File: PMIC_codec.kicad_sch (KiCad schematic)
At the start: 18 parts, among them U5 RK809-2

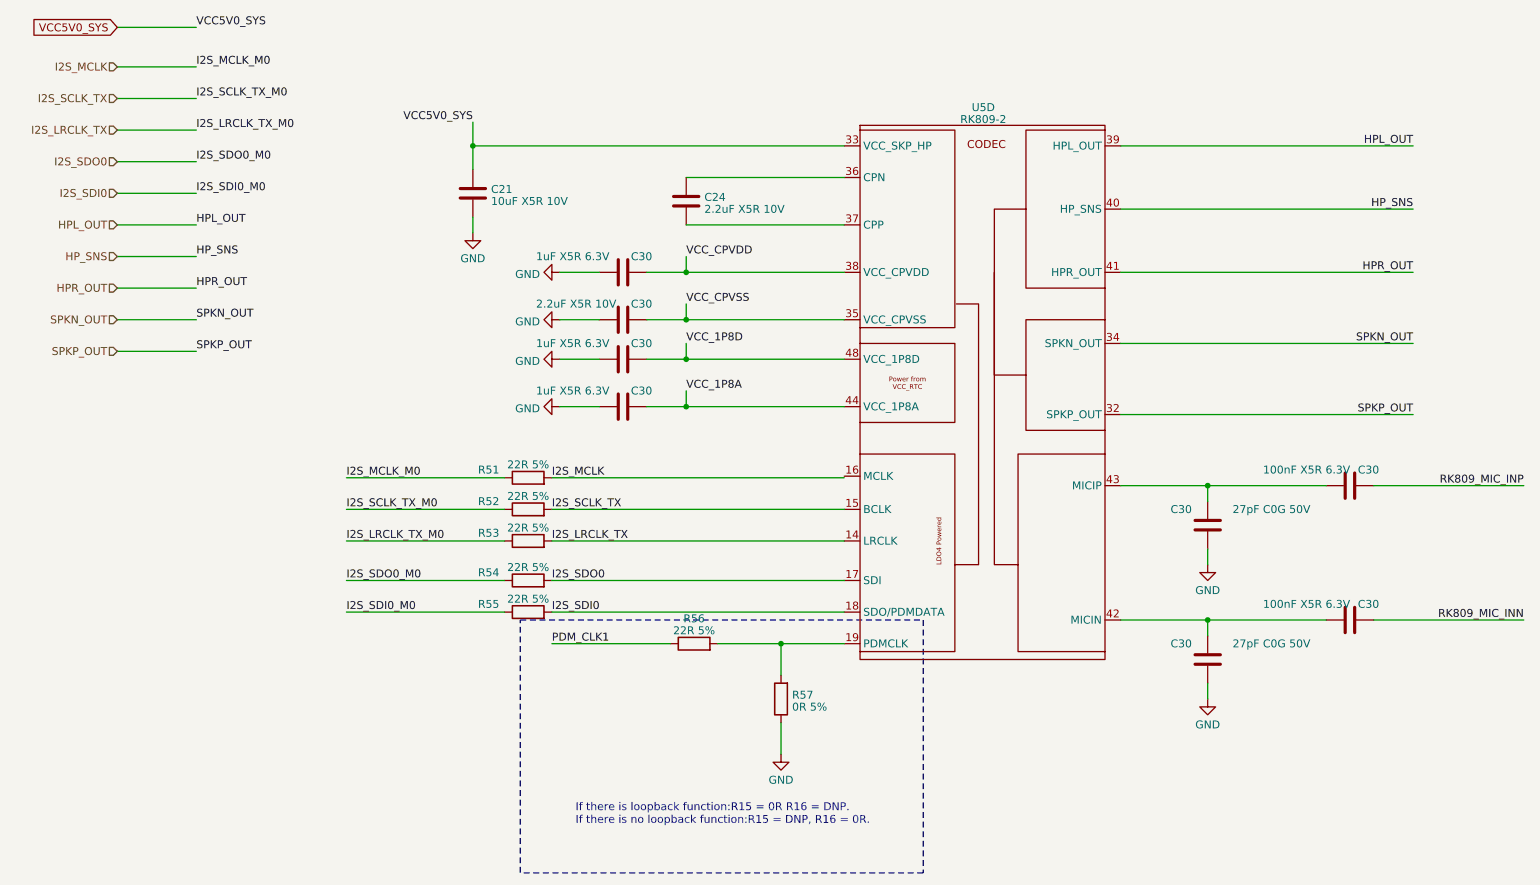
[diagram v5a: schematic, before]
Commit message: fix some ERCs
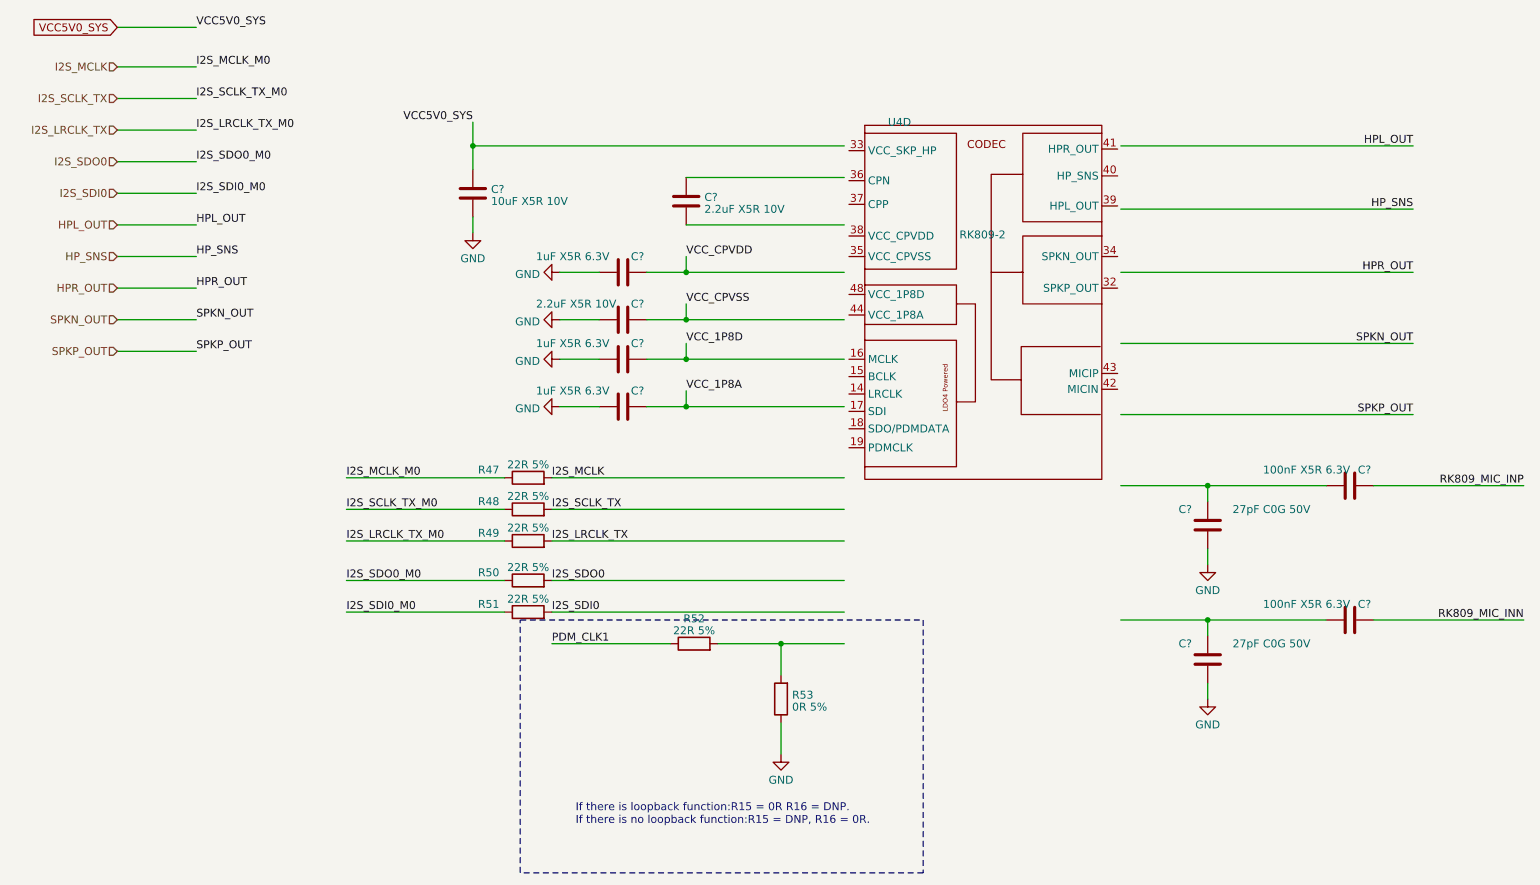
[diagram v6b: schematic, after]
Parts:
- renumbered C30 to C?, C21 to C?, C24 to C?, R51 to R47, R52 to R48, R53 to R49, R54 to R50, R55 to R51, R56 to R52, R57 to R53, U5 to U4
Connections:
- net HPL_OUT: no longer U4.39 (HPL_OUT)
- net HPR_OUT: no longer U4.41 (HPR_OUT)
- net HP_SNS: no longer U4.40 (HP_SNS)
- net I2S_LRCLK_TX: no longer U4.14 (LRCLK)
- net I2S_SCLK_TX: no longer U4.15 (BCLK)
- net I2S_SDI0: no longer U4.18 (SDO/PDMDATA)
- net I2S_SDO0: no longer U4.17 (SDI)
- net SPKN_OUT: no longer U4.34 (SPKN_OUT)
- net SPKP_OUT: no longer U4.32 (SPKP_OUT)
- net VCC5V0_SYS: no longer U4.33 (VCC_SKP_HP)
- net VCC_1P8A: no longer U4.44 (VCC_1P8A)
- net VCC_1P8D: no longer U4.48 (VCC_1P8D)
- net VCC_CPVDD: no longer U4.38 (VCC_CPVDD)
- net VCC_CPVSS: no longer U4.35 (VCC_CPVSS)
- net at R52.2, R53.2: no longer U4.19 (PDMCLK)
- net at U4.36 (CPN): no longer C?.1
- net at U4.37 (CPP): no longer C?.2
- net at C?.1, C?.2: no longer U4.42 (MICIN)
- net at C?.1, C?.2: no longer U4.43 (MICIP)

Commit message: fix ERC
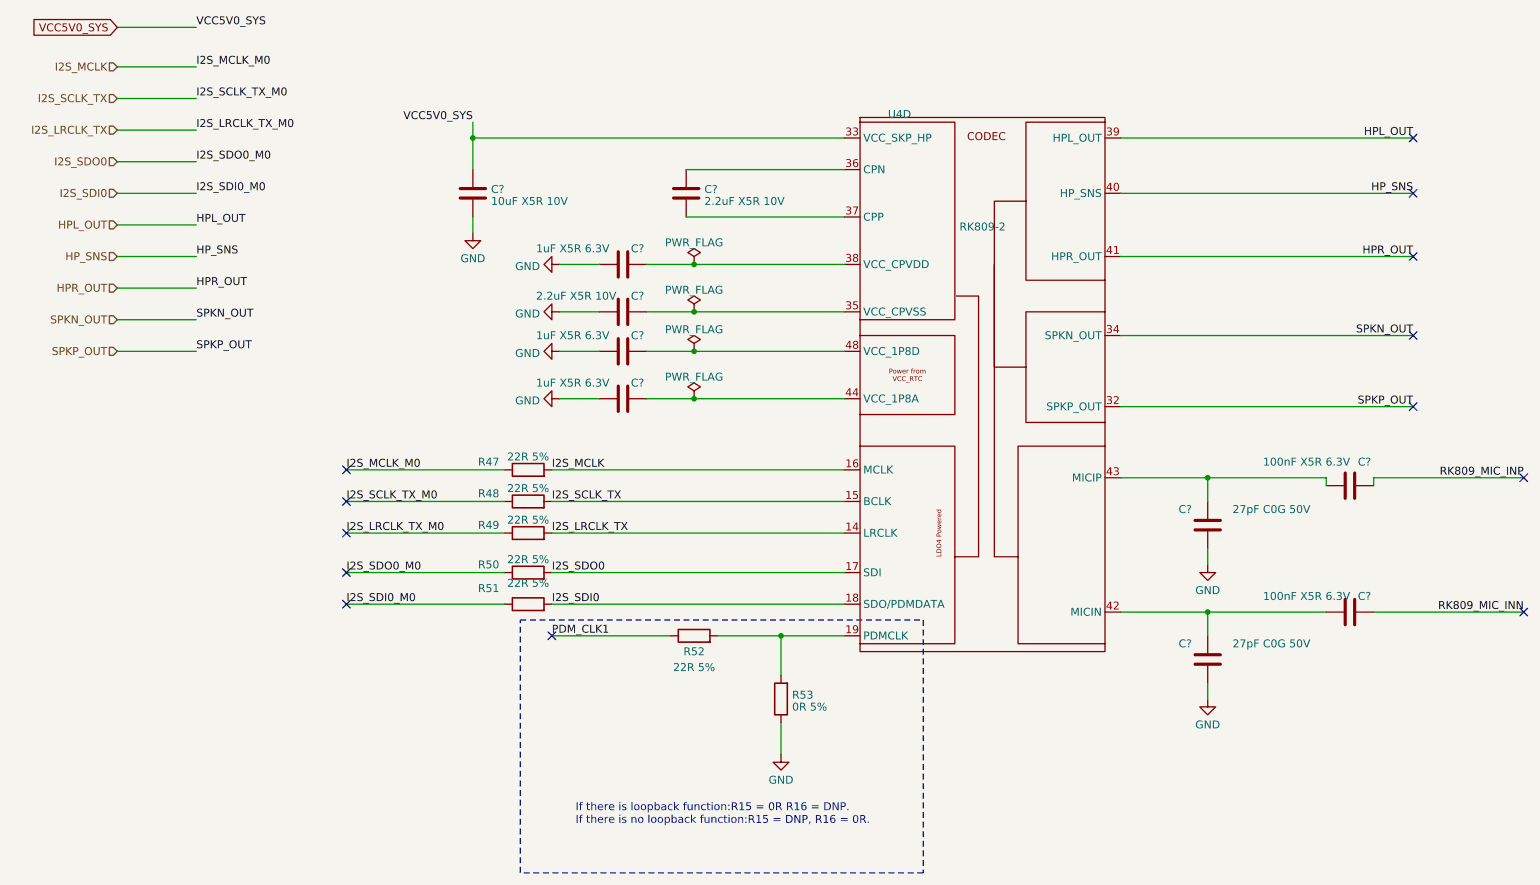
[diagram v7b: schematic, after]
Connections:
- net VCC_1P8A is gone; now on an unnamed net: C?.1
- net VCC_1P8D is gone; now on an unnamed net: C?.1
- net VCC_CPVDD is gone; now on an unnamed net: C?.1
- net VCC_CPVSS is gone; now on an unnamed net: C?.1
- net HPL_OUT: now also U4.39 (HPL_OUT)
- net HPR_OUT: now also U4.41 (HPR_OUT)
- net HP_SNS: now also U4.40 (HP_SNS)
- net I2S_LRCLK_TX: now also U4.14 (LRCLK)
- net I2S_MCLK: now also U4.16 (MCLK)
- net I2S_SCLK_TX: now also U4.15 (BCLK)
- net I2S_SDI0: now also U4.18 (SDO/PDMDATA)
- net I2S_SDO0: now also U4.17 (SDI)
- net SPKN_OUT: now also U4.34 (SPKN_OUT)
- net SPKP_OUT: now also U4.32 (SPKP_OUT)
- net VCC5V0_SYS: now also U4.33 (VCC_SKP_HP)
- net at U4.19 (PDMCLK): now also R52.2, R53.2
- net at U4.36 (CPN): now also C?.1
- net at U4.37 (CPP): now also C?.2
- net at U4.42 (MICIN): now also C?.1, C?.2
- net at U4.43 (MICIP): now also C?.1, C?.2
- no-connect marks 0 -> 13
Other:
- moved on the sheet: C?, R47, R48, R49, R50, R51, R52

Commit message: updated symbols
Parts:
- R53: LCSC (none) -> C17168; Model (none) -> 0402WGF0000TCE; Vendor (none) -> UNI-ROYAL(厚声)
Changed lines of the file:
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@@
+      (effects (font (size 1.27 1.27)) hide)
+    )
+    (property "Description" "电阻类型: 厚膜电阻 阻值: 0Ω 精度: ±1% 功率: 1/16W 温度系数: ±800ppm/℃ 最大工作电压: 50V 工作" (at 144.78 130.81 0)
+      (effects (font (size 1.27 1.27)) hide)
+    )
+    (property "LCSC" "C17168" (at 144.78 130.81 0)
+      (effects (font (size 1.27 1.27)) hide)
+    )
+    (property "Model" "0402WGF0000TCE" (at 144.78 130.81 0)
+      (effects (font (size 1.27 1.27)) hide)
+    )
+    (property "Vendor" "UNI-ROYAL(厚声)" (at 144.78 130.81 0)
       (effects (font (size 1.27 1.27)) hide)
     )
